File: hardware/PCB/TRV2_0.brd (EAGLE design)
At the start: 46 x 70 mm, 55 parts, among them IC1 TMP112, IC2 SHT21, IC3 APDS-9300-020, IC4 CNY70, IC5 ATMEGA8-AU, Q1 FC-12M

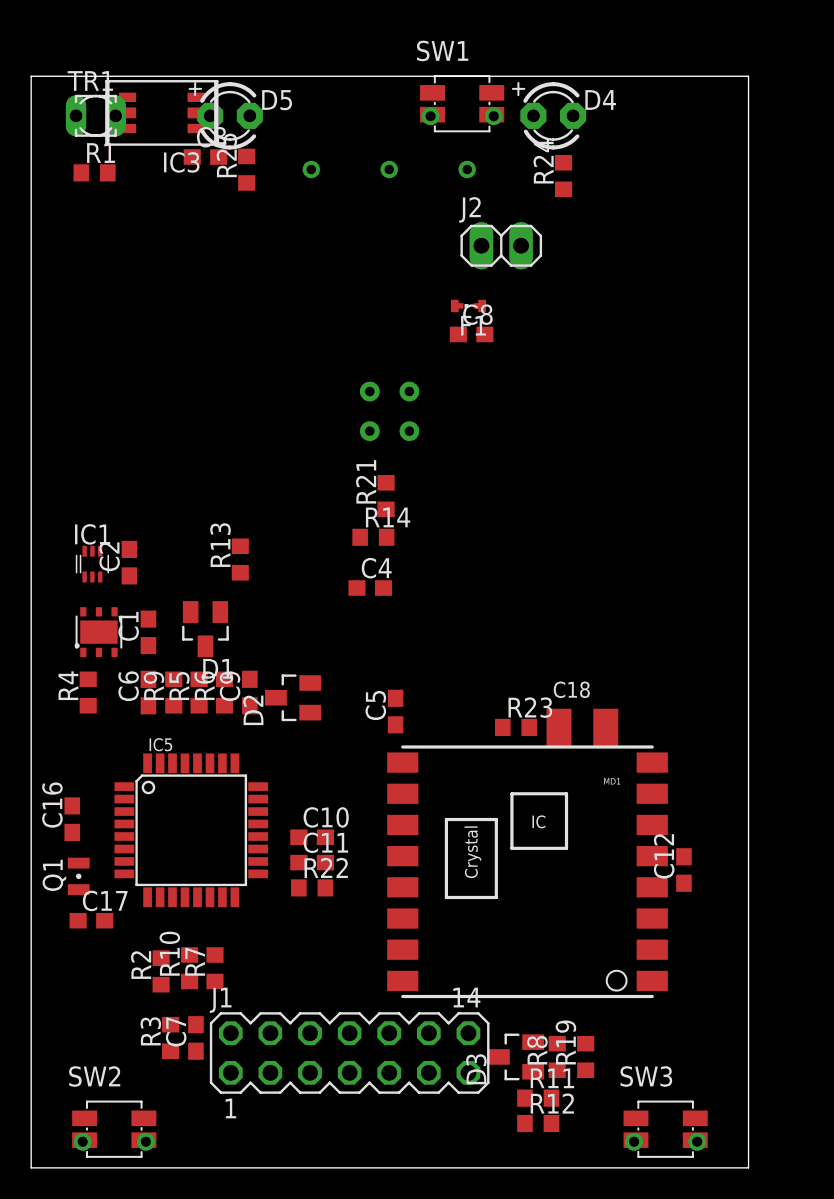
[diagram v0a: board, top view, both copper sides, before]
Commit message: Componets rotated and locked
locked as they now point the same way as the one made by enlight
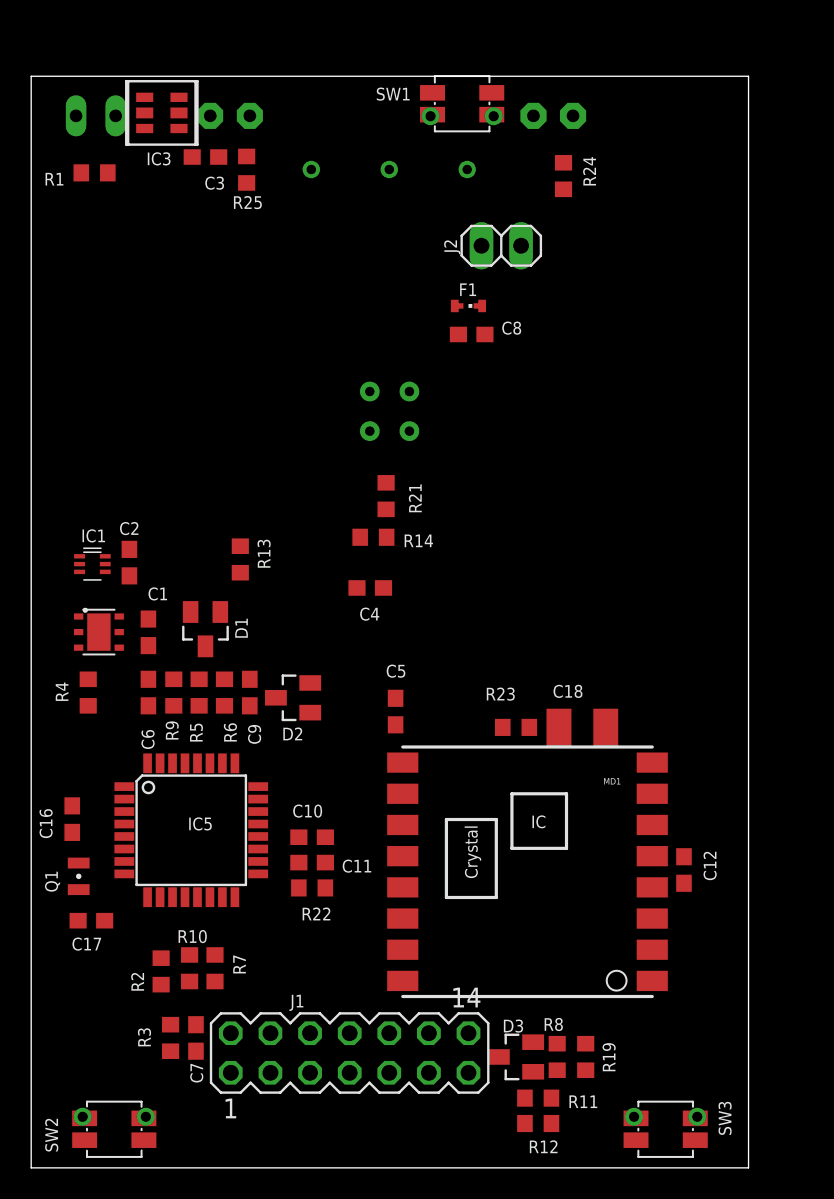
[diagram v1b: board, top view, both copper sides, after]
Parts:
- turned C1 to 270 degrees
- turned C12 to 270 degrees
- turned C2 to 270 degrees
- turned C3 to 180 degrees
- turned C4 to 180 degrees
- turned C6 to 270 degrees
- turned C7 to 270 degrees
- turned C9 to 270 degrees
- flipped D4 to the bottom, turned to 180 degrees
- flipped D5 to the bottom, turned to 180 degrees
- turned F1 to 270 degrees
- turned IC1 to 270 degrees
- turned IC2 to 270 degrees
- turned Q1 to 270 degrees
- turned R1 to 180 degrees
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
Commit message: added motor header
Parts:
- removed D4: Green, adafruit:LED3MM
- removed R24: 470R, resistor:R0603
- removed R3, R4: 4K7, resistor:R0603
- removed SW2, SW3: (no value), EAGLE-TACT_SWITCHES-rev16e:434331013822
- added J4: (no value), pinhead:1X02
- C16, C17: value 22P -> 0p
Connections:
- removed net BUTTON_LEARN2_L: IC5.1, R4.1, SW3.1
- removed net BUTTON_LEARN_L: IC5.12, R3.1, SW2.1
- removed net N$6: D4.K, R24.1
- net GND: no longer SW2.3, SW2.5, SW3.3, SW3.5
- net SPI_SCLK: now also IC5.17; no longer R24.2
- net VCC: no longer D4.A, R3.2, R4.2

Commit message: cleaned up
Issues this far

>>>- We don't want the RFM23B on this model (Damon, do we want to keep
the footprint?)
>>>- We want TR1 and D5 to be SMD devices with the 'active' side on the
top edge of the board.
>>>-Why does comms connector not use our standard 100%? pin8 was not
labeled at all and one more had a different name
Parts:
- removed C3: 100N, rcl:C0603
- removed IC3: APDS-9300-020, APDS-9300-020:APDS-9300-020
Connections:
- removed net INT: IC3.P$6
- net GND: no longer C3.2, IC3.P$2, IC3.P$3
- net SCL: no longer IC3.P$4
- net SDA: no longer IC3.P$5
- net VCC: no longer C3.1, IC3.P$1
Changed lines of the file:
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@@
 <attribute name="NAME" x="5.6388" y="40.5892" size="0.8128" layer="25"/>
-</element>
-<element name="C3" library="rcl" package="C0603" value="100N" x="11.176" y="64.8208" locked="yes" smashed="yes" rot="R180">
-<attribute name="NAME" x="12.446" y="63.5508" size="0.8128" layer="25" rot="R180"/>
 </element>
 <element name="C4" library="rcl" package="C0603" value="100N" x="21.7424" y="37.1856" locked="yes" smashed="yes" rot="R180">
@@
 </element>
 <element name="IC2" library="SHT21" package="SHT21" value="SHT21" x="4.344796875" y="34.356803125" locked="yes" smashed="yes" rot="R270"/>
-<element name="IC3" library="APDS-9300-020" package="APDS-9300-020" value="APDS-9300-020" x="8.378596875" y="67.649596875" locked="yes" smashed="yes">
-<attribute name="MF" value="" x="8.378596875" y="67.649596875" size="1.778" layer="27" display="off"/>
-<attribute name="MPN" value="" x="8.378596875" y="67.649596875" size="1.778" layer="27" display="off"/>
-<attribute name="OC_FARNELL" value="unknown" x="8.378596875" y="67.649596875" size="1.778" layer="27" display="off"/>
-<attribute name="OC_NEWARK" value="unknown" x="8.378596875" y="67.649596875" size="1.778" layer="27" display="off"/>
-<attribute name="NAME" x="9.013596875" y="65.109596875" size="0.8128" layer="25" ratio="10" rot="R180"/>
-</element>
 <element name="IC4" library="cny70" package="4" value="CNY70" x="22.984003125" y="48.514" locked="yes" smashed="yes" rot="MR0">
 <attribute name="NAME" x="27.575" y="49.781003125" size="0.8128" layer="26" ratio="10" rot="MR270"/>
@@
 <contactref element="C1" pad="1"/>
 <contactref element="VR1" pad="3"/>
-<contactref element="C3" pad="1"/>
 <contactref element="D3" pad="2"/>
 <contactref element="R8" pad="2"/>
@@
 <contactref element="IC5" pad="6"/>
 <contactref element="R9" pad="1"/>
-<contactref element="IC3" pad="P$1"/>
 <wire x1="27.1666" y1="55.2704" x2="27.9616" y2="64.0207" width="0" layer="19" extent="1-1"/>
 <wire x1="27.3948" y1="53.4416" x2="27.1666" y2="55.2704" width="0" layer="19" extent="1-1"/>
-<wire x1="12.026" y1="64.8208" x2="27.9616" y2="64.0207" width="0" layer="19" extent="1-1"/>
-<wire x1="11.4808" y1="67.4624" x2="12.026" y2="64.8208" width="0" layer="19" extent="1-1"/>
-<wire x1="7.278596875" y1="68.649596875" x2="11.4808" y2="67.4624" width="0" layer="19" extent="1-1"/>
+<wire x1="11.4808" y1="67.4624" x2="27.9616" y2="64.0207" width="0" layer="19" extent="1-1"/>
 <wire x1="13.4112" y1="39.8644" x2="27.3948" y2="53.4416" width="0" layer="19" extent="1-1"/>
 <wire x1="10.226" y1="35.644" x2="13.4112" y2="39.8644" width="0" layer="19" extent="1-1"/>
@@
 <contactref element="C4" pad="2"/>
 <contactref element="R1" pad="1"/>
-<contactref element="C3" pad="2"/>
 <contactref element="D3" pad="1"/>
 <contactref element="D1" pad="1"/>
@@
 <contactref element="IC5" pad="5"/>
 <contactref element="IC5" pad="21"/>
-<contactref element="IC3" pad="P$3"/>
-<contactref element="IC3" pad="P$2"/>
 <wire x1="25.6102" y1="67.4379875" x2="29.5352" y2="67.5379875" width="0" layer="19" extent="1-1"/>
 <wire x1="17.9616" y1="64.0207" x2="25.6102" y2="67.4379875" width="0" layer="19" extent="1-1"/>
-<wire x1="10.326" y1="64.8208" x2="17.9616" y2="64.0207" width="0" layer="19" extent="1-1"/>
-<wire x1="7.278596875" y1="66.649596875" x2="10.326" y2="64.8208" width="0" layer="19" extent="1-1"/>
-<wire x1="7.278596875" y1="67.649596875" x2="7.278596875" y2="66.649596875" width="0" layer="19" extent="1-1"/>
-<wire x1="4.914" y1="63.8048" x2="7.278596875" y2="66.649596875" width="0" layer="19" extent="1-1"/>
 <wire x1="31.414390625" y1="59.1312" x2="29.5352" y2="67.5379875" width="0" layer="19" extent="1-1"/>
 <wire x1="29.0948" y1="53.4416" x2="31.414390625" y2="59.1312" width="0" layer="19" extent="1-1"/>
@@
 <wire x1="41.8592" y1="18.2508" x2="39.827190625" y2="13.9888125" width="0" layer="19" extent="1-1"/>
 <wire x1="36.8441" y1="28.2448" x2="41.8592" y2="18.2508" width="0" layer="19" extent="1-1"/>
+<wire x1="4.914" y1="63.8048" x2="17.9616" y2="64.0207" width="0" layer="19" extent="1-1"/>
 </signal>
 <signal name="SCL">
@@
 <contactref element="J1" pad="9"/>
 <contactref element="IC5" pad="28"/>
-<contactref element="IC3" pad="P$4"/>
-<wire x1="3.10120625" y1="39.2176" x2="9.478596875" y2="66.649596875" width="0" layer="19" extent="1-1"/>
-<wire x1="5.644796875" y1="35.356803125" x2="3.10120625" y2="39.2176" width="0" layer="19" extent="1-1"/>
-<wire x1="11.176" y1="33.444" x2="5.644796875" y2="35.356803125" width="0" layer="19" extent="1-1"/>
 <wire x1="10.7696" y1="29.63" x2="11.176" y2="33.444" width="0" layer="19" extent="1-1"/>
 <wire x1="10.66360625" y1="25.941603125" x2="10.7696" y2="29.63" width="0" layer="19" extent="1-1"/>
+<wire x1="5.644796875" y1="35.356803125" x2="11.176" y2="33.444" width="0" layer="19" extent="1-1"/>
+<wire x1="3.10120625" y1="39.2176" x2="5.644796875" y2="35.356803125" width="0" layer="19" extent="1-1"/>
 <wire x1="22.9616" y1="6.096" x2="10.66360625" y2="25.941603125" width="0" layer="19" extent="1-1"/>
 </signal>
@@
 <contactref element="J1" pad="10"/>
 <contactref element="IC5" pad="27"/>
-<contactref element="IC3" pad="P$5"/>
-<wire x1="4.75120625" y1="39.2176" x2="9.478596875" y2="67.649596875" width="0" layer="19" extent="1-1"/>
-<wire x1="3.044796875" y1="35.356803125" x2="4.75120625" y2="39.2176" width="0" layer="19" extent="1-1"/>
-<wire x1="12.3952" y1="29.63" x2="3.044796875" y2="35.356803125" width="0" layer="19" extent="1-1"/>
-<wire x1="15.6950125" y1="30.143196875" x2="12.3952" y2="29.63" width="0" layer="19" extent="1-1"/>
+<wire x1="12.3952" y1="29.63" x2="15.6950125" y2="30.143196875" width="0" layer="19" extent="1-1"/>
 <wire x1="11.46360625" y1="25.941603125" x2="12.3952" y2="29.63" width="0" layer="19" extent="1-1"/>
+<wire x1="3.044796875" y1="35.356803125" x2="12.3952" y2="29.63" width="0" layer="19" extent="1-1"/>
+<wire x1="4.75120625" y1="39.2176" x2="3.044796875" y2="35.356803125" width="0" layer="19" extent="1-1"/>
 <wire x1="22.9616" y1="8.636" x2="11.46360625" y2="25.941603125" width="0" layer="19" extent="1-1"/>
 </signal>
@@
 <contactref element="IC5" pad="26"/>
 </signal>
-<signal name="INT">
-<contactref element="IC3" pad="P$6"/>
-</signal>
 </signals>

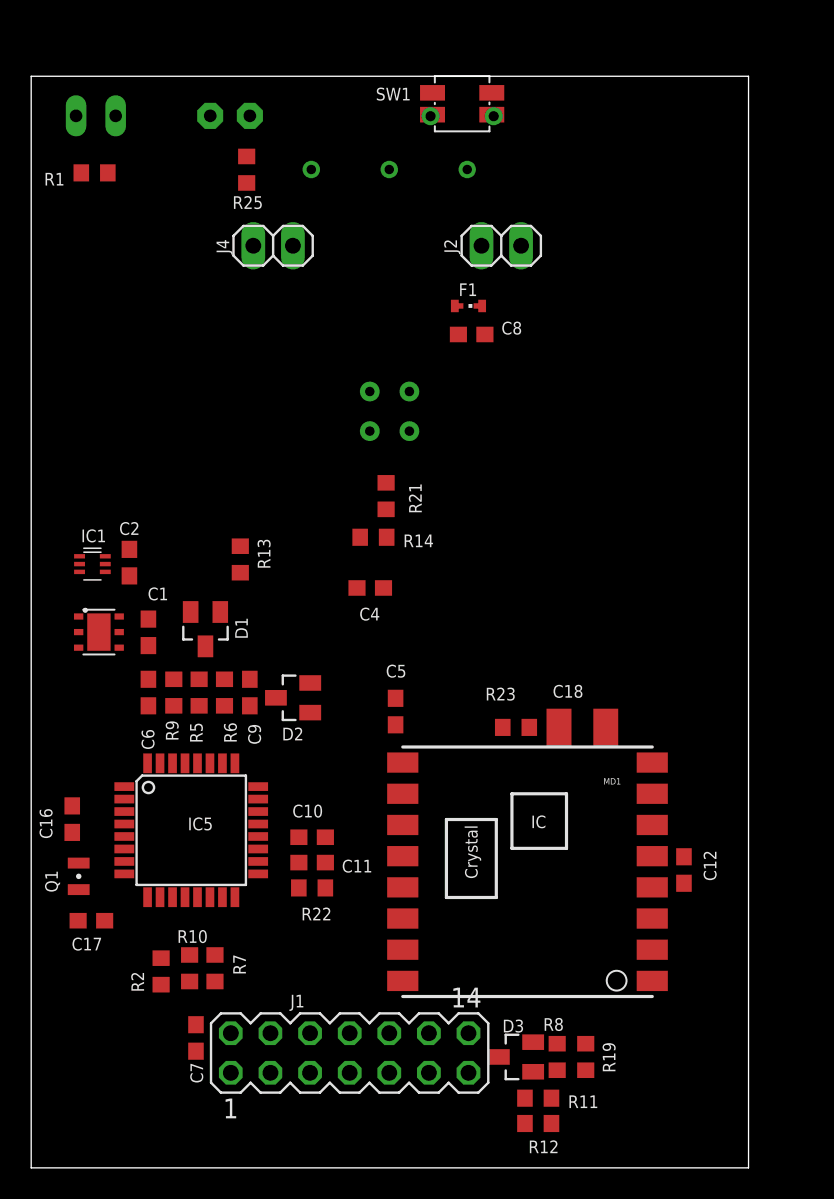
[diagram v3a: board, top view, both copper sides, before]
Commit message: removed RFM
8 pin header is just placeholder for now
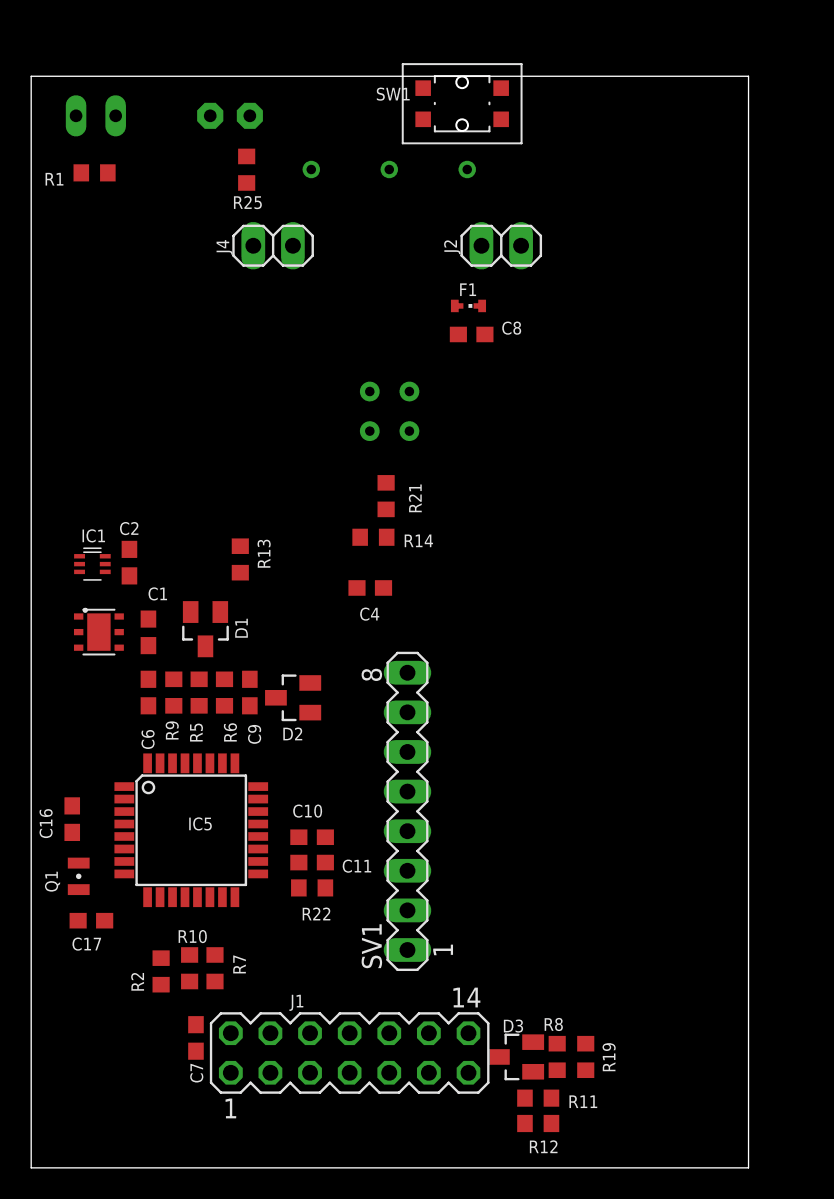
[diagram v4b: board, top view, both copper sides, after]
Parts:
- removed C12, C5: 100N, rcl:C0603
- removed C18: 10uF 6V, resistor:SMC_B
- removed MD1: RFM23B, SparkFun-RF:RFM23-XXX-S1
- removed R23: 1R0, resistor:R0603
- added SV1: (no value), con-lstb:MA08-1
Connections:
- removed net N$2: J1.8
- net ANT: now also SV1.8; no longer MD1.1
- net BOILER: no longer J1.7
- net GND: now also SV1.7; no longer C12.2, C18.-, C5.2, MD1.15, MD1.16, MD1.2, MD1.9, SW1.5
- net N$3: now also SV1.2; no longer MD1.14
- net RFMIRQ: now also J1.7
- net RFVCC: now also SV1.1; no longer C12.1, C18.+, MD1.5, R23.1
- net SPI_MISO: now also SV1.6; no longer MD1.10
- net SPI_MOSI: now also SV1.5; no longer MD1.11
- net SPI_NNS: now also J1.8, SV1.3; no longer MD1.13
- net SPI_SCLK: now also SV1.4; no longer MD1.12
- net VCC: no longer C5.1, R23.2

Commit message: SMD LED and photo added
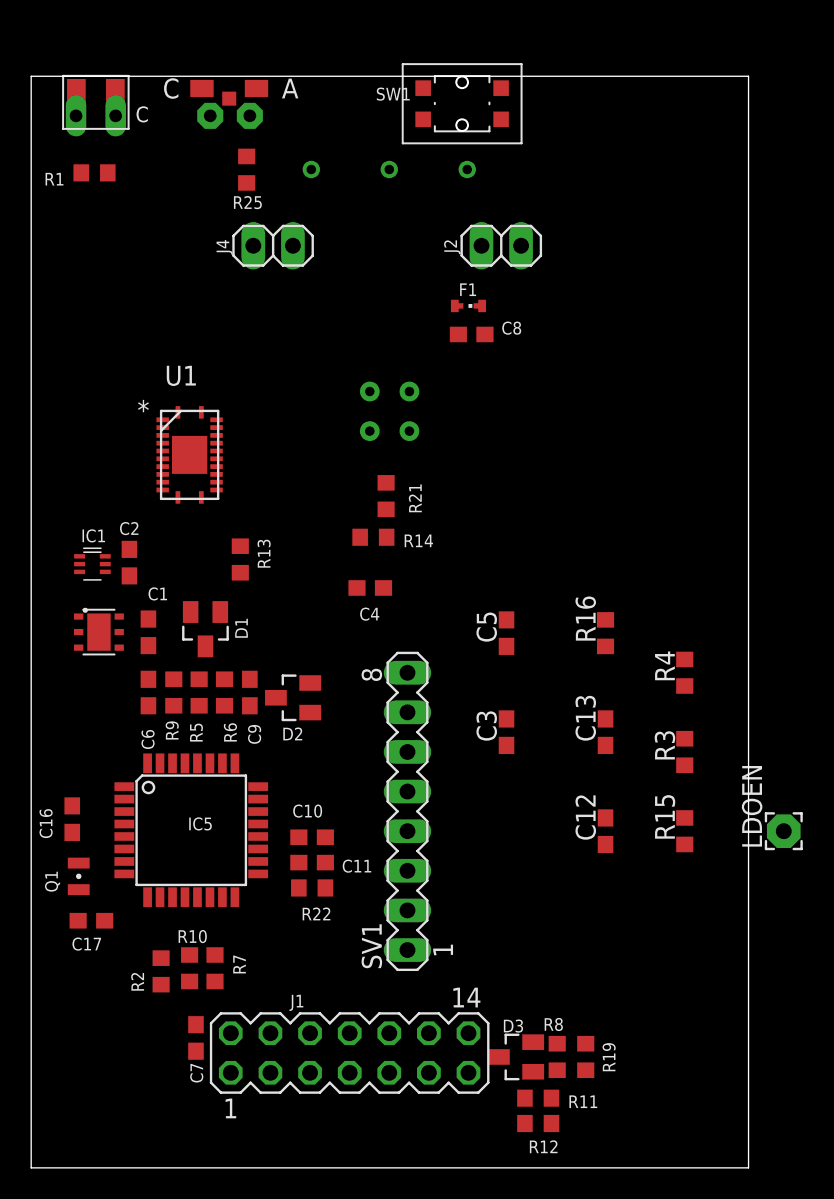
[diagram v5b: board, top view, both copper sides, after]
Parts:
- added C12, C5: 0.1uF, resistor:C0603
- added C13: 10uF, resistor:C0603
- added C3: 2.2uF, resistor:C0603
- added LDOEN: WIREPAD2,15/1,0, wirepad:2,15/1,0
- added R15: 1K, resistor:R0603
- added R16: 4.3K, resistor:R0603
- added R3: 24K, resistor:R0603
- added R4: 3K, resistor:R0603
- added U$1: SFH_325-3/4, opto-trans-siemens:SFH_325-3/4
- added U$2: KINGBRIGHTSIDELED, led:KINGBRIGHTSIDELED
- added U1: DRV8850_RGY_24, drv8850:RGY_24
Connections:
- new net A1: R16.2, U1.16
- new net D3: U1.5
- new net D5: U1.7
- new net D6: U1.6
- new net D7: U1.8
- new net N$11: J4.1, U1.21, U1.22, U1.23
- new net N$12: R3.2, U1.11
- new net N$14: R15.2, R4.1, U1.14
- new net N$15: C3.1, R4.2, U1.15
- new net N$16: LDOEN.1, U1.10
- new net N$2: J4.2, U1.2, U1.3, U1.4
- new net N$20: C5.2, U1.17
- new net VCC1: C12.2, C13.2, C5.1, U1.18, U1.19, U1.20
- net GND: now also C12.1, C13.1, C3.2, R15.1, R16.1, R3.1, U1.1, U1.12, U1.13, U1.24, U1.25
- net IO_POWER_UP: now also U$1.P$2, U1.9
- net LDR: now also U$1.P$1
- net N$7: now also U$2.C
- net VCC: now also U$2.A
